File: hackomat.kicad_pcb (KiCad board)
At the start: 2 copper layers, 95 x 90 mm, 54 parts, among them IC1 MOC3021M, IC10 MOC3021M, IC11 MOC3021M, IC12 MOC3021M, IC13 MOC3021M, IC14 MOC3021M, IC15 MOC3021M, IC16 MOC3021M, IC17 MOC3021M, IC18 MOC3021M, IC19 MOC3021M, IC2 MOC3021M, IC20 MOC3021M, IC21 MOC3021M, IC22 MOC3021M, IC23 MOC3021M, IC24 MOC3021M, IC25 MOC3021M, IC26 MOC3021M, IC27 MOC3021M, IC28 MOC3021M, IC29 MOC3021M, IC3 MOC3021M, IC30 MOC3021M, IC31 MOC3021M, IC32 MOC3021M, IC33 MOC3021M, IC34 MOC3021M, IC35 MOC3021M, IC36 MOC3021M, IC37 MOC3021M, IC38 MOC3021M, IC39 MOC3021M, IC4 MOC3021M, IC40 MOC3021M, IC41 MOC3021M, IC42 MOC3021M, IC5 MOC3021M, IC6 MOC3021M, IC7 MOC3021M, IC8 MOC3021M, IC9 MOC3021M, J1 RJ45, P1 CONN_02X22, P2 CONN_02X08, P35 CONN_01X01, P36 CONN_01X01, P42 CONN_01X01

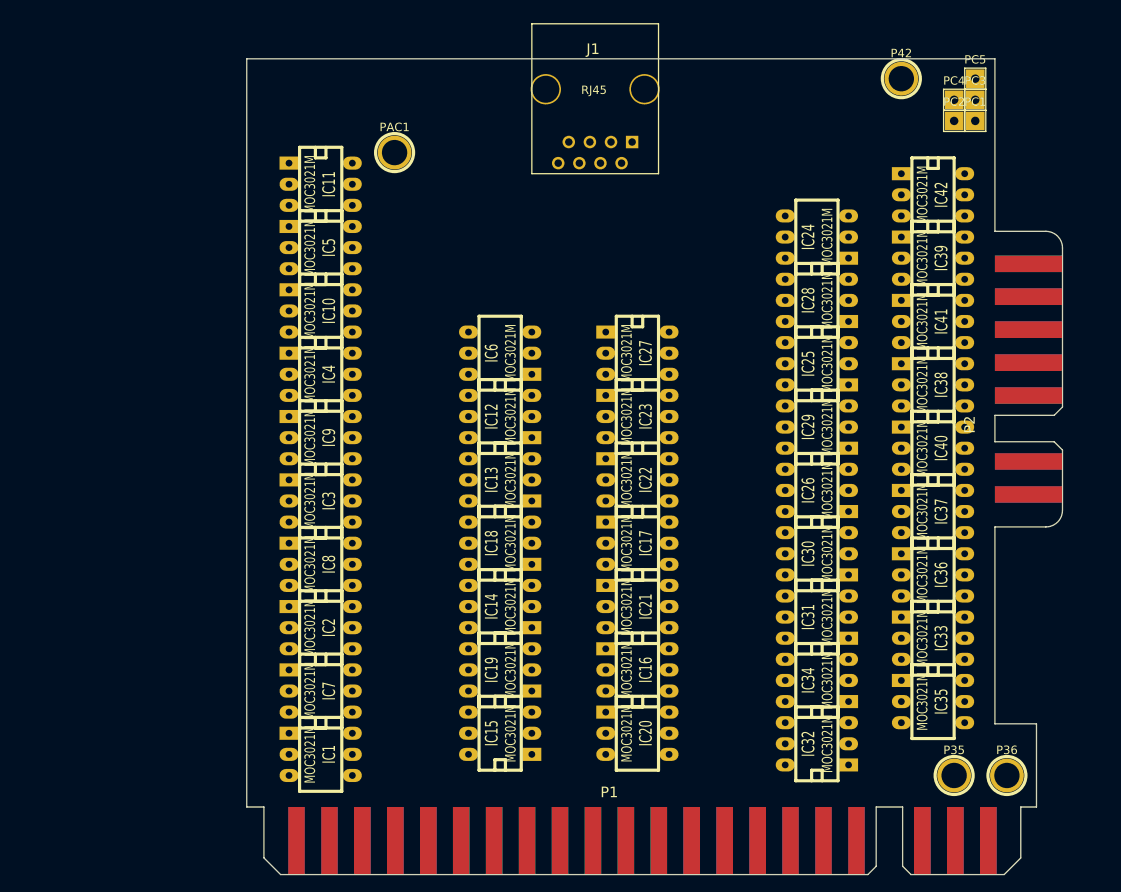
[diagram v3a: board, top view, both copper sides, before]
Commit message: wire up about half the AC wires to triacs
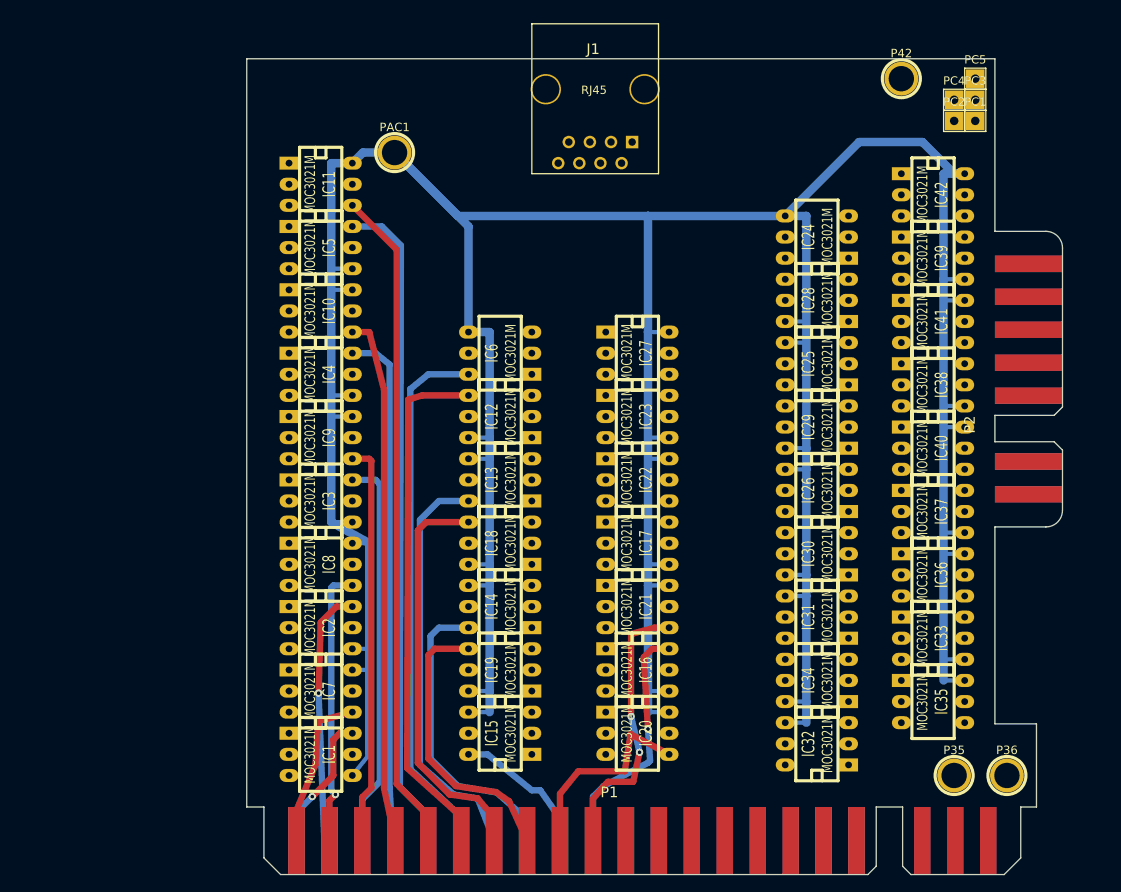
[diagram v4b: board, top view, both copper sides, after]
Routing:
- net /ac: track 0.00 -> 514.9 mm
- net /mo10: track 0.00 -> 80.2 mm
- net /mo9: track 0.00 -> 79.8 mm
- net /mo11: track 0.00 -> 64.6 mm
- net /mo8: track 0.00 -> 63.6 mm
- net /mo12: track 0.00 -> 63.2 mm
- net /mo7: track 0.00 -> 62.0 mm
- net /mo13: track 0.00 -> 50.0 mm
- net /mo14: track 0.00 -> 49.1 mm
- net /mo6: track 0.00 -> 48.5 mm
- net /mo5: track 0.00 -> 47.3 mm
- net /mo15: track 0.00 -> 36.6 mm
- net /mo16: track 0.00 -> 34.3 mm
- net /mo4: track 0.00 -> 33.6 mm, vias 0 -> 1
- net /mo20: track 0.00 -> 33.5 mm, vias 0 -> 2
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
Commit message: almost all the rj45 data pins, all the other traces
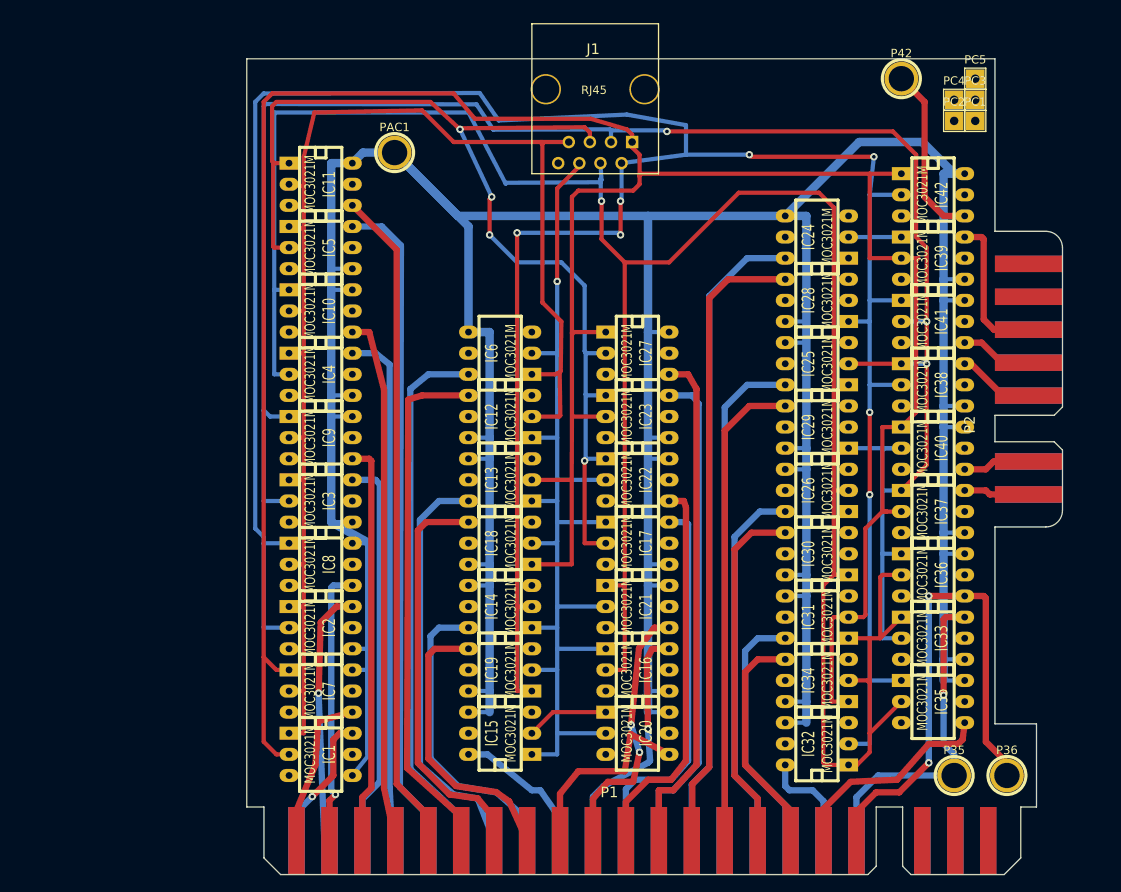
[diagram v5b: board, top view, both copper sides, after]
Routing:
- net /b: track 0.00 -> 335.3 mm, vias 0 -> 7
- net /a: track 0.00 -> 321.8 mm
- net /d: track 0.00 -> 292.5 mm, vias 0 -> 1
- net /c: track 0.00 -> 239.6 mm, vias 0 -> 3
- net /g: track 0.00 -> 166.0 mm
- net /e: track 0.00 -> 131.4 mm, vias 0 -> 4
- net /f: track 0.00 -> 123.6 mm, vias 0 -> 1
- net /mo25: track 0.00 -> 77.4 mm
- net /mo26: track 0.00 -> 76.2 mm
- net /mo36: track 0.00 -> 64.0 mm, vias 0 -> 2
- net /mo24: track 0.00 -> 61.5 mm
- net /mo27: track 0.00 -> 60.5 mm
- net /mo23: track 0.00 -> 59.5 mm
- net /mo28: track 0.00 -> 57.8 mm
- net /mo22: track 0.00 -> 47.2 mm
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
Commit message: board is finished thanx to substack
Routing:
- net /c: track 239.6 -> 340.7 mm, vias 3 -> 12
- net /e: track 131.4 -> 223.6 mm, vias 4 -> 6
- net /g: track 166.0 -> 170.5 mm

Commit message: fixed some white lines, then rayc touched it, watch out
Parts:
- moved P42 2.18 mm to (237.0, 73.7)
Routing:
- net /mo42: track 21.2 -> 22.4 mm
- net /b: track 335.3 -> 334.8 mm
